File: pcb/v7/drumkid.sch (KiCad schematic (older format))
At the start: 54 parts, among them J1 DIN-5_180degree, J2 DIN-5_180degree, J3 Conn_01x15, J4 Conn_01x15, J9 AudioJack3_Ground_Switch, SW1 SW_Push, SW2 SW_Push, SW3 SW_Push, SW4 SW_Push, SW5 SW_Push, SW6 SW_Push, SW7 SW_SPDT, SW8 SW_SPDT, U1 6N138

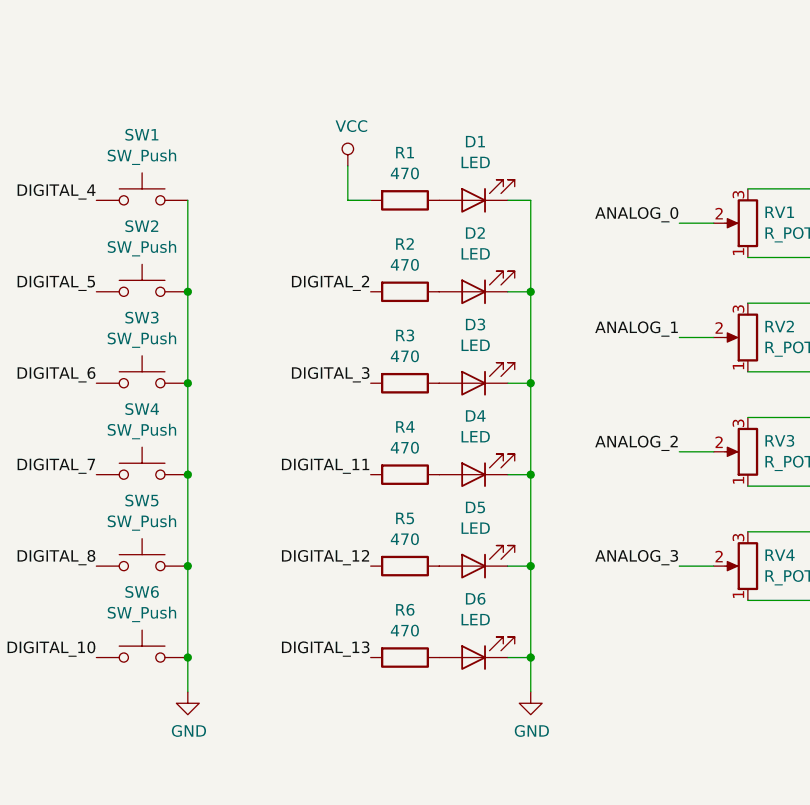
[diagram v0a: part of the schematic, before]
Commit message: added BOM
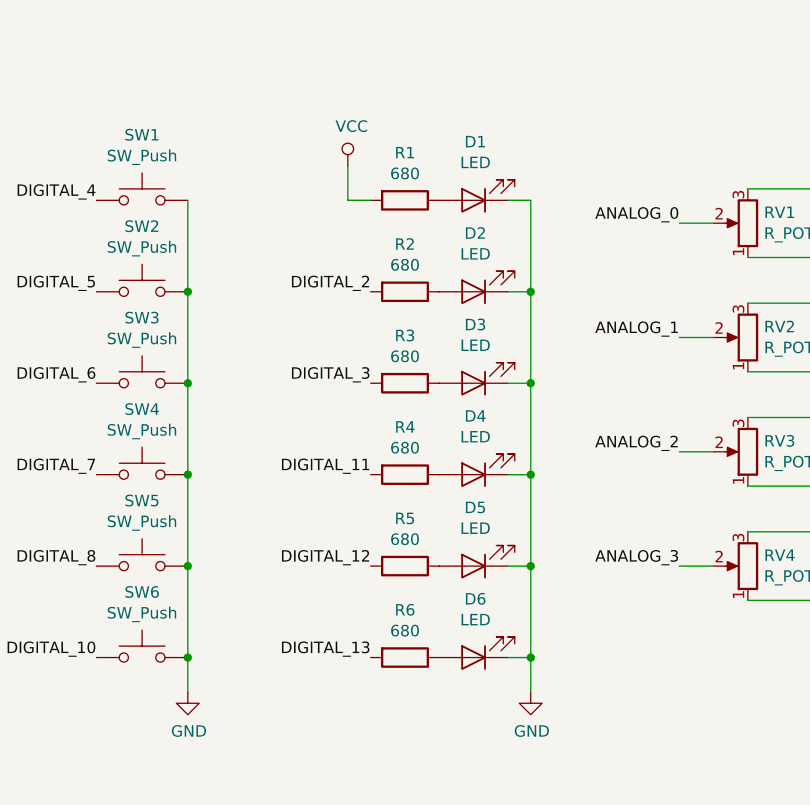
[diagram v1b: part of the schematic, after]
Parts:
- R1, R2, R3, R4, R5, R6: value 470 -> 680
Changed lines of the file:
@@
 P 5450 2050
 F 0 "R2" V 5243 2050 50  0000 C CNN
-F 1 "470" V 5334 2050 50  0000 C CNN
+F 1 "680" V 5334 2050 50  0000 C CNN
 F 2 "drumkidcustom:R_Axial_DIN0207_L6.3mm_D2.5mm_P10.16mm_Horizontal" V 5380 2050 50  0001 C CNN
 F 3 "~" H 5450 2050 50  0001 C CNN
@@
 P 5450 2450
 F 0 "R3" V 5243 2450 50  0000 C CNN
-F 1 "470" V 5334 2450 50  0000 C CNN
+F 1 "680" V 5334 2450 50  0000 C CNN
 F 2 "drumkidcustom:R_Axial_DIN0207_L6.3mm_D2.5mm_P10.16mm_Horizontal" V 5380 2450 50  0001 C CNN
 F 3 "~" H 5450 2450 50  0001 C CNN
@@
 P 5450 2850
 F 0 "R4" V 5243 2850 50  0000 C CNN
-F 1 "470" V 5334 2850 50  0000 C CNN
+F 1 "680" V 5334 2850 50  0000 C CNN
 F 2 "drumkidcustom:R_Axial_DIN0207_L6.3mm_D2.5mm_P10.16mm_Horizontal" V 5380 2850 50  0001 C CNN
 F 3 "~" H 5450 2850 50  0001 C CNN
@@
 P 5450 3250
 F 0 "R5" V 5243 3250 50  0000 C CNN
-F 1 "470" V 5334 3250 50  0000 C CNN
+F 1 "680" V 5334 3250 50  0000 C CNN
 F 2 "drumkidcustom:R_Axial_DIN0207_L6.3mm_D2.5mm_P10.16mm_Horizontal" V 5380 3250 50  0001 C CNN
 F 3 "~" H 5450 3250 50  0001 C CNN
@@
 P 5450 3650
 F 0 "R6" V 5243 3650 50  0000 C CNN
-F 1 "470" V 5334 3650 50  0000 C CNN
+F 1 "680" V 5334 3650 50  0000 C CNN
 F 2 "drumkidcustom:R_Axial_DIN0207_L6.3mm_D2.5mm_P10.16mm_Horizontal" V 5380 3650 50  0001 C CNN
 F 3 "~" H 5450 3650 50  0001 C CNN
@@
 P 5450 1650
 F 0 "R1" V 5243 1650 50  0000 C CNN
-F 1 "470" V 5334 1650 50  0000 C CNN
+F 1 "680" V 5334 1650 50  0000 C CNN
 F 2 "drumkidcustom:R_Axial_DIN0207_L6.3mm_D2.5mm_P10.16mm_Horizontal" V 5380 1650 50  0001 C CNN
 F 3 "~" H 5450 1650 50  0001 C CNN
